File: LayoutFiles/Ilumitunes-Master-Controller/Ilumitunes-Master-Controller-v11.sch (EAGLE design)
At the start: 13 parts, among them U1 ARDUINO_SHIELD

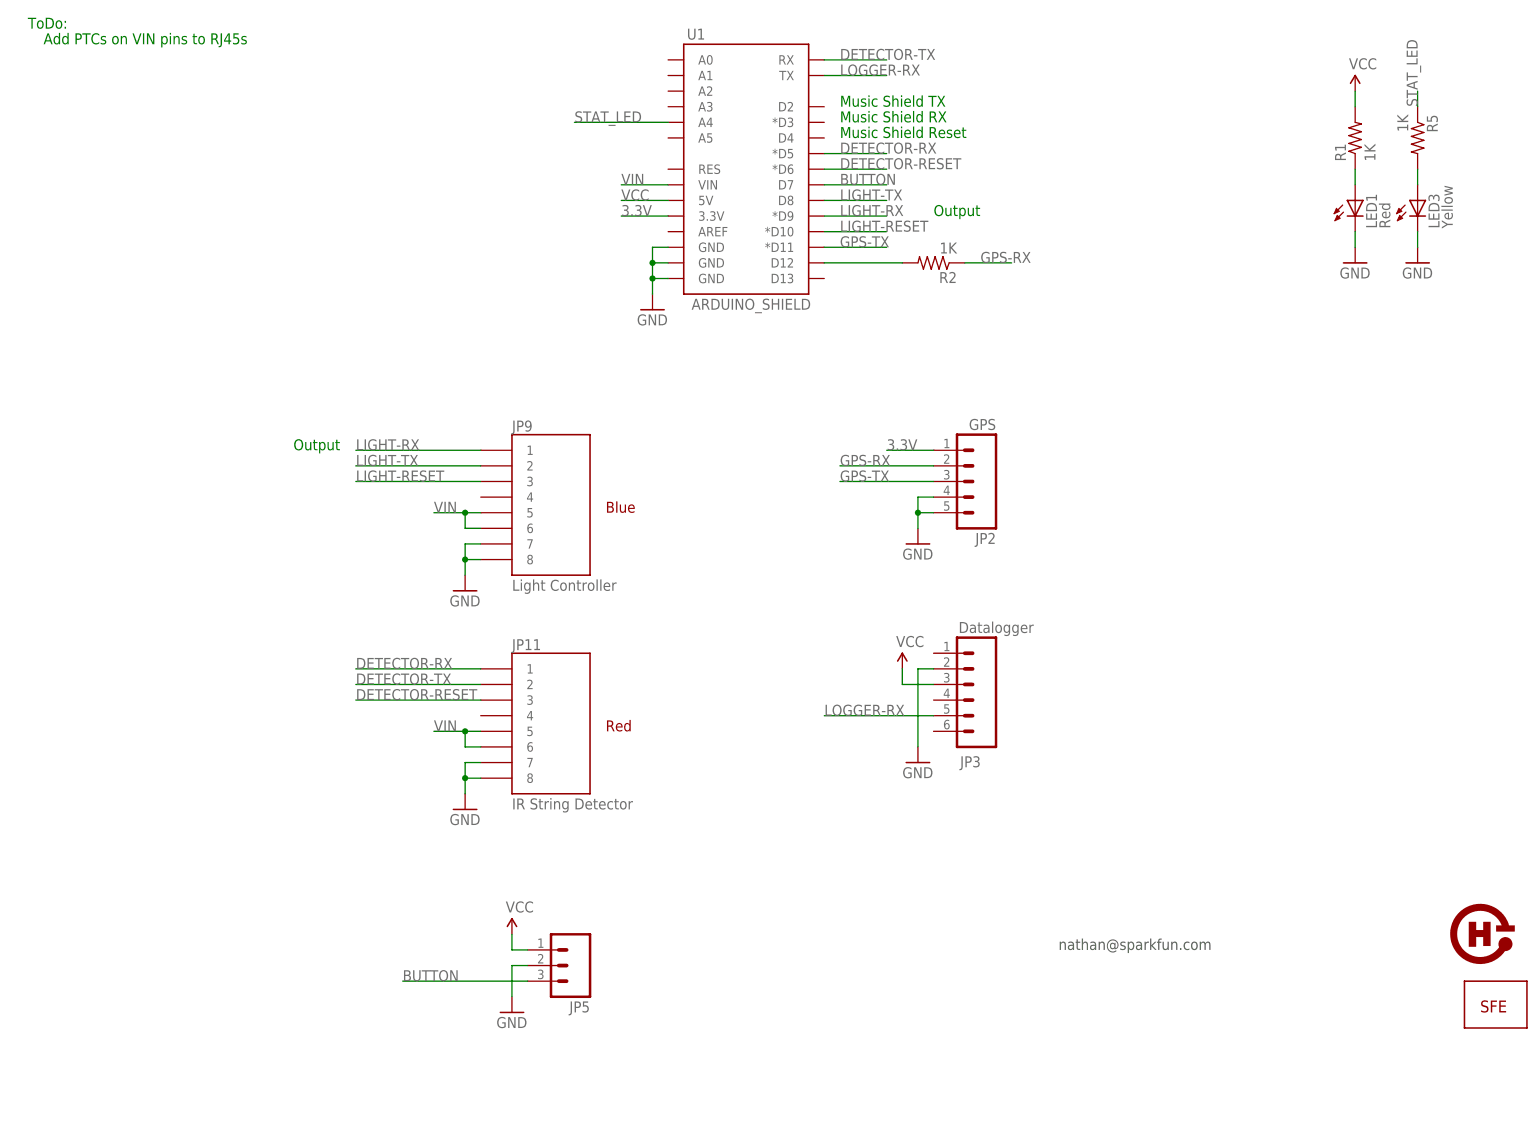
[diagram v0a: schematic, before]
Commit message: Added more PTC and decoupling to string controller at breakout.
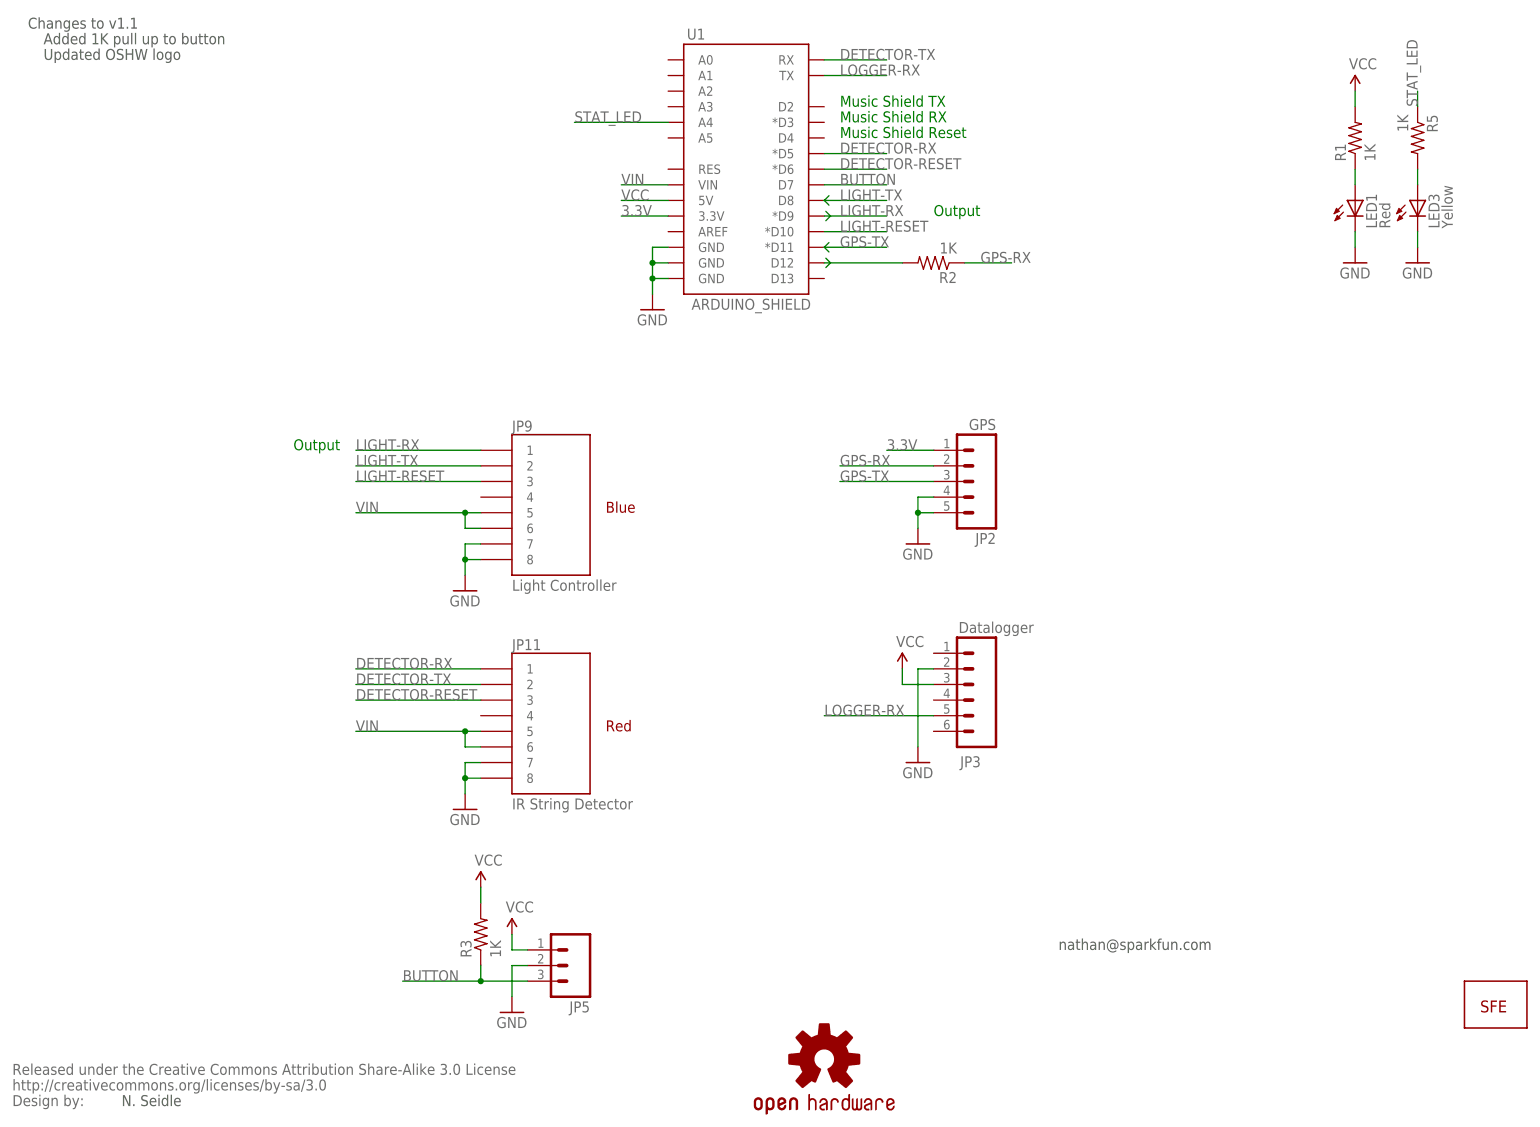
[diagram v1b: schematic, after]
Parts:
- added R3: 1K, SparkFun-Passives:RESISTORAXIAL-0.3
- added U$3: OSHW-LOGOS, SparkFun-Aesthetics:OSHW-LOGOS
- U$2: value OSHW-LOGO -> CREATIVE_COMMONS; device SparkFun:OSHW-LOGO -> SparkFun-Aesthetics:CREATIVE_COMMONS
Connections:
- net BUTTON: now also R3.1
- net VCC: now also R3.2
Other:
- note added: "Added 1K pull up to button"
- note added: "Changes to v1.1"
- note added: "N. Seidle"
- note added: "Updated OSHW logo"
- note removed: "Add PTCs on VIN pins to RJ45s"
- note removed: "ToDo:"
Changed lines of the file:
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@@
 <layer number="121" name="_tsilk" color="7" fill="1" visible="yes" active="yes"/>
 <layer number="122" name="_bsilk" color="7" fill="1" visible="yes" active="yes"/>
+<layer number="125" name="_tNames" color="7" fill="1" visible="no" active="yes"/>
 <layer number="144" name="Drill_legend" color="7" fill="1" visible="yes" active="yes"/>
 <layer number="151" name="HeatSink" color="7" fill="1" visible="yes" active="yes"/>
@@
 <layer number="215" name="215bmp" color="7" fill="1" visible="yes" active="yes"/>
 <layer number="216" name="216bmp" color="7" fill="1" visible="yes" active="yes"/>
+<layer number="217" name="217bmp" color="18" fill="1" visible="no" active="no"/>
+<layer number="218" name="218bmp" color="19" fill="1" visible="no" active="no"/>
+<layer number="219" name="219bmp" color="20" fill="1" visible="no" active="no"/>
+<layer number="220" name="220bmp" color="21" fill="1" visible="no" active="no"/>
+<layer number="221" name="221bmp" color="22" fill="1" visible="no" active="no"/>
+<layer number="222" name="222bmp" color="23" fill="1" visible="no" active="no"/>
+<layer number="223" name="223bmp" color="24" fill="1" visible="no" active="no"/>
+<layer number="224" name="224bmp" color="25" fill="1" visible="no" active="no"/>
 <layer number="250" name="Descript" color="7" fill="1" visible="no" active="no"/>
 <layer number="251" name="SMDround" color="7" fill="1" visible="no" active="no"/>
@@
 <part name="JP9" library="SparkFun" deviceset="RJ45-8" device="PTH" value="Light Controller"/>
 <part name="JP5" library="SparkFun" deviceset="M03" device="JST-PTH-VERT"/>
-<part name="U$2" library="SparkFun" deviceset="OSHW-LOGO" device=""/>
 <part name="GND1" library="SparkFun" deviceset="GND" device=""/>
 <part name="GND2" library="SparkFun" deviceset="GND" device=""/>
@@
 <part name="GND4" library="SparkFun" deviceset="GND" device=""/>
 <part name="R2" library="SparkFun" deviceset="RESISTOR" device="AXIAL-0.3" value="1K"/>
+<part name="U$3" library="SparkFun-Aesthetics" deviceset="OSHW-LOGO" device="S"/>
+<part name="U$2" library="SparkFun-Aesthetics" deviceset="CREATIVE_COMMONS" device=""/>
+<part name="R3" library="SparkFun-Passives" deviceset="RESISTOR" device="AXIAL-0.3" value="1K"/>
+<part name="P+3" library="SparkFun" deviceset="VCC" device=""/>
 </parts>
 <sheets>
@@
 <text x="48.26" y="109.22" size="1.778" layer="91">Output</text>
 <text x="172.72" y="27.94" size="1.778" layer="97">nathan@sparkfun.com</text>
-<text x="7.62" y="175.26" size="1.778" layer="91">Add PTCs on VIN pins to RJ45s</text>
-<text x="5.08" y="177.8" size="1.778" layer="91">ToDo:</text>
+<text x="5.08" y="177.8" size="1.778" layer="97">Changes to v1.1</text>
+<text x="20.32" y="2.54" size="1.778" layer="97">N. Seidle</text>
+<text x="7.62" y="175.26" size="1.778" layer="97">Added 1K pull up to button</text>
+<text x="7.62" y="172.72" size="1.778" layer="97">Updated OSHW logo</text>
 </plain>
 <instances>
@@
 <instance part="JP9" gate="G$1" x="91.44" y="99.06"/>
 <instance part="JP5" gate="G$1" x="93.98" y="25.4" rot="R180"/>
-<instance part="U$2" gate="G$1" x="236.22" y="25.4"/>
 <instance part="GND1" gate="1" x="106.68" y="132.08"/>
 <instance part="GND2" gate="1" x="83.82" y="17.78"/>
@@
 <instance part="GND4" gate="1" x="149.86" y="93.98"/>
 <instance part="R2" gate="G$1" x="152.4" y="139.7" rot="R180"/>
+<instance part="U$3" gate="G$1" x="134.62" y="10.16"/>
+<instance part="U$2" gate="G$1" x="2.54" y="2.54"/>
+<instance part="R3" gate="G$1" x="78.74" y="30.48" rot="R90"/>
+<instance part="P+3" gate="1" x="78.74" y="38.1"/>
 </instances>
 <busses>
@@
 <pinref part="P+2" gate="1" pin="VCC"/>
 </segment>
+<segment>
+<pinref part="R3" gate="G$1" pin="2"/>
+<pinref part="P+3" gate="1" pin="VCC"/>
+<wire x1="78.74" y1="38.1" x2="78.74" y2="35.56" width="0.1524" layer="91"/>
+</segment>
 </net>
 <net name="N$4" class="0">
@@
 <net name="VIN" class="0">
 <segment>
-<wire x1="78.74" y1="63.5" x2="76.2" y2="63.5" width="0.1524" layer="91"/>
-<wire x1="76.2" y1="63.5" x2="71.12" y2="63.5" width="0.1524" layer="91"/>
-<wire x1="78.74" y1="60.96" x2="76.2" y2="60.96" width="0.1524" layer="91"/>
-<wire x1="76.2" y1="63.5" x2="76.2" y2="60.96" width="0.1524" layer="91"/>
-<junction x="76.2" y="63.5"/>
-<label x="71.12" y="63.5" size="1.778" layer="95"/>
-<pinref part="JP11" gate="G$1" pin="5"/>
-<pinref part="JP11" gate="G$1" pin="6"/>
-</segment>
-<segment>
-<wire x1="78.74" y1="99.06" x2="76.2" y2="99.06" width="0.1524" layer="91"/>
-<wire x1="76.2" y1="99.06" x2="71.12" y2="99.06" width="0.1524" layer="91"/>
-<wire x1="78.74" y1="96.52" x2="76.2" y2="96.52" width="0.1524" layer="91"/>
-<wire x1="76.2" y1="99.06" x2="76.2" y2="96.52" width="0.1524" layer="91"/>
-<junction x="76.2" y="99.06"/>
-<label x="71.12" y="99.06" size="1.778" layer="95"/>
-<pinref part="JP9" gate="G$1" pin="5"/>
-<pinref part="JP9" gate="G$1" pin="6"/>
-</segment>
-<segment>
 <wire x1="109.22" y1="152.4" x2="101.6" y2="152.4" width="0.1524" layer="91"/>
 <label x="101.6" y="152.4" size="1.778" layer="95"/>
 <pinref part="U1" gate="G$1" pin="VIN"/>
 </segment>
+<segment>
+<pinref part="JP11" gate="G$1" pin="5"/>
+<wire x1="78.74" y1="63.5" x2="76.2" y2="63.5" width="0.1524" layer="91"/>
+<pinref part="JP11" gate="G$1" pin="6"/>
+<wire x1="76.2" y1="63.5" x2="58.42" y2="63.5" width="0.1524" layer="91"/>
+<wire x1="78.74" y1="60.96" x2="76.2" y2="60.96" width="0.1524" layer="91"/>
+<wire x1="76.2" y1="60.96" x2="76.2" y2="63.5" width="0.1524" layer="91"/>
+<junction x="76.2" y="63.5"/>
+<label x="58.42" y="63.5" size="1.778" layer="95"/>
+</segment>
+<segment>
+<pinref part="JP9" gate="G$1" pin="6"/>
+<wire x1="78.74" y1="96.52" x2="76.2" y2="96.52" width="0.1524" layer="91"/>
+<wire x1="76.2" y1="96.52" x2="76.2" y2="99.06" width="0.1524" layer="91"/>
+<wire x1="76.2" y1="99.06" x2="58.42" y2="99.06" width="0.1524" layer="91"/>
+<pinref part="JP9" gate="G$1" pin="5"/>
+<wire x1="78.74" y1="99.06" x2="76.2" y2="99.06" width="0.1524" layer="91"/>
+<junction x="76.2" y="99.06"/>
+<label x="58.42" y="99.06" size="1.778" layer="95"/>
+</segment>
 </net>
 <net name="DETECTOR-TX" class="0">
@@
 <net name="BUTTON" class="0">
 <segment>
-<wire x1="66.04" y1="22.86" x2="86.36" y2="22.86" width="0.1524" layer="91"/>
+<wire x1="66.04" y1="22.86" x2="78.74" y2="22.86" width="0.1524" layer="91"/>
 <label x="66.04" y="22.86" size="1.778" layer="95"/>
 <pinref part="JP5" gate="G$1" pin="3"/>
+<pinref part="R3" gate="G$1" pin="1"/>
+<wire x1="78.74" y1="22.86" x2="86.36" y2="22.86" width="0.1524" layer="91"/>
+<wire x1="78.74" y1="25.4" x2="78.74" y2="22.86" width="0.1524" layer="91"/>
+<junction x="78.74" y="22.86"/>
 </segment>
 <segment>
@@
 </segment>
 <segment>
-<wire x1="134.62" y1="147.32" x2="144.78" y2="147.32" width="0.1524" layer="91"/>
+<wire x1="135.636" y1="139.7" x2="134.874" y2="140.462" width="0.2032" layer="91"/>
+<wire x1="135.636" y1="139.7" x2="134.874" y2="138.938" width="0.2032" layer="91"/>
+</segment>
+<segment>
+<wire x1="134.62" y1="147.32" x2="135.636" y2="147.32" width="0.1524" layer="91"/>
 <label x="137.16" y="147.32" size="1.778" layer="95"/>
 <pinref part="U1" gate="G$1" pin="*D9"/>
+<wire x1="135.636" y1="147.32" x2="144.78" y2="147.32" width="0.1524" layer="91"/>
+<wire x1="135.636" y1="147.32" x2="134.874" y2="148.082" width="0.2032" layer="91"/>
+<wire x1="135.636" y1="147.32" x2="134.874" y2="146.558" width="0.2032" layer="91"/>
 </segment>
 </net>
@@
 </segment>
 </net>
+<net name="N$2" class="0">
+<segment>
+<wire x1="134.62" y1="149.86" x2="135.382" y2="150.622" width="0.2032" layer="91"/>
+<wire x1="134.62" y1="149.86" x2="135.382" y2="149.098" width="0.2032" layer="91"/>
+<wire x1="134.62" y1="142.24" x2="135.382" y2="141.478" width="0.2032" layer="91"/>
+<wire x1="134.62" y1="142.24" x2="135.382" y2="143.002" width="0.2032" layer="91"/>
+</segment>
+</net>
